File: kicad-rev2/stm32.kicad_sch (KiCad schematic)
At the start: 45 parts, among them J2 USB_C_Receptacle_USB2.0, J3 SWD, M1 Fan_4pin, SW1 boot, U1 LM1117-3.3, U2 STM32L072KZT6, U4 TMP1075, U5 TXU0101

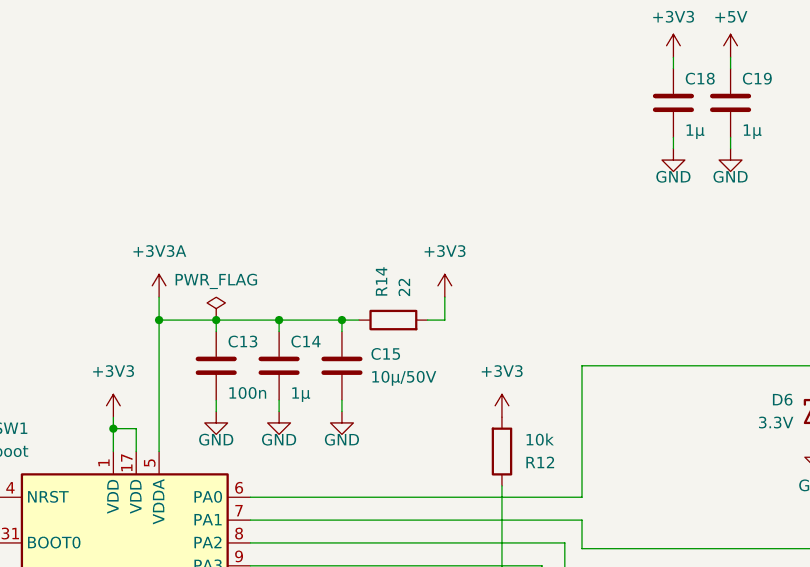
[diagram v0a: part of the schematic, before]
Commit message: set 22R to 0R (fix for adc)
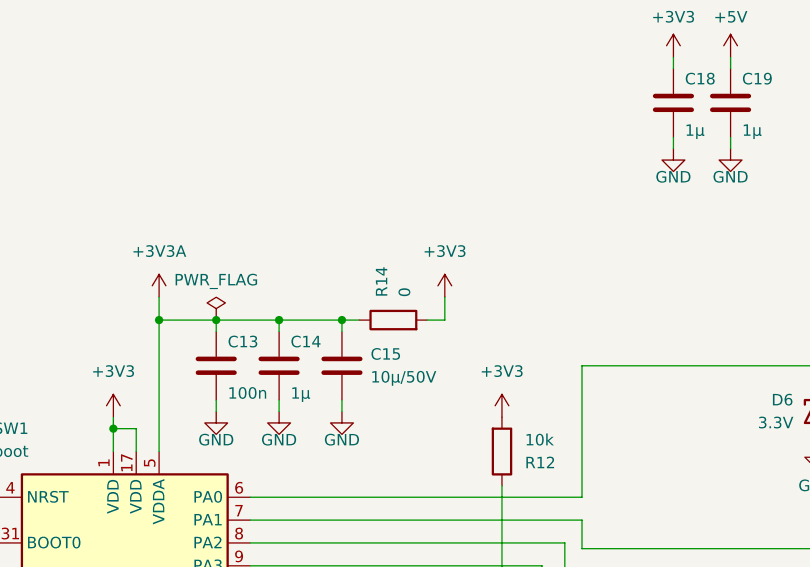
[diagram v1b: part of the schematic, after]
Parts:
- R14: value 22 -> 0
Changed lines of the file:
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@@
 			)
 		)
-		(property "Value" "22"
+		(property "Value" "0"
 			(at 147.32 75.565 0)
 			(effects
